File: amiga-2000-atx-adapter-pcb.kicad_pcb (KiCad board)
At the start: 2 copper layers, 99.9 x 63.8 mm, 33 parts, among them J1 ATX-24, J121 12V, J18 PU-18, J2 5.25" PWR, J20 A2000 Power, J21 3.5" PWR, J22 3.5" PWR, J23 3.5" PWR, J24 3.5" PWR, J3 PWR ON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

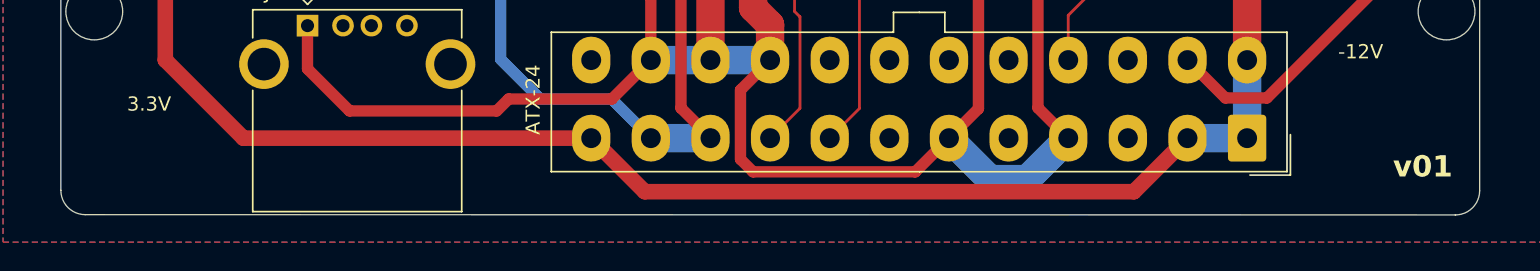
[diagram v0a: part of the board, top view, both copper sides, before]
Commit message: v02: Add ground pad
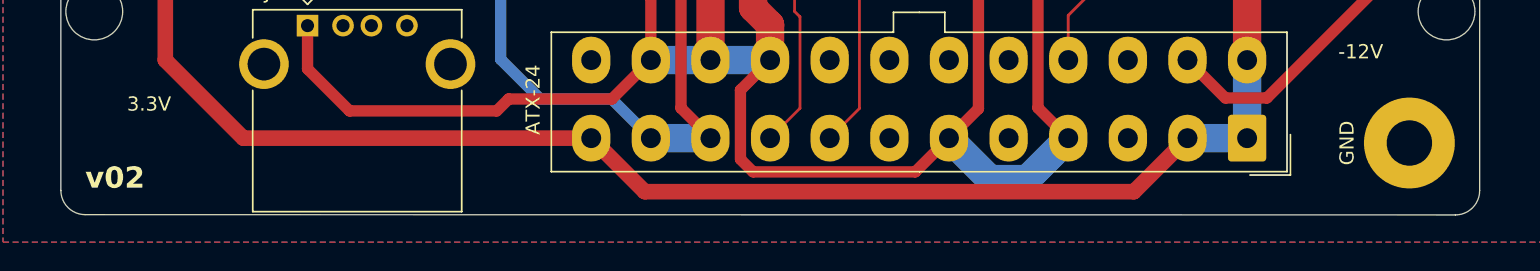
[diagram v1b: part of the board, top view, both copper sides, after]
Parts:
- added H5: MountingHole_Pad, MountingHole:MountingHole_3.2mm_M3_Pad, F.Cu at (218.4, 132.1)
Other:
- board text added: "GND"
- board text added: "v02"
- board text removed: "v01"
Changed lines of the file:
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@@
 		)
 	)
+	(footprint "MountingHole:MountingHole_3.2mm_M3_Pad"
+		(layer "F.Cu")
+		(at 218.44 132.08)
+		(descr "Mounting Hole 3.2mm, M3")
+		(tags "mounting hole 3.2mm m3")
+		(property "Reference" "H5"
+			(at 0 -4.2 0)
+			(layer "F.SilkS")
+			(hide yes)
+			(effects
+				(font
+					(size 1 1)
+					(thickness 0.15)
+				)
+			)
+		)
+		(property "Value" "MountingHole_Pad"
+			(at 0 4.2 0)
+			(layer "F.Fab")
+			(hide yes)
+			(effects
+				(font
+					(size 1 1)
+					(thickness 0.15)
+				)
+			)
+		)
+		(property "Footprint" "MountingHole:MountingHole_3.2mm_M3_Pad"
+			(at 0 0 0)
+			(unlocked yes)
+			(layer "F.Fab")
+			(hide yes)
+			(effects
+				(font
+					(size 1.27 1.27)
+					(thickness 0.15)
+				)
+			)
+		)
+		(property "Datasheet" ""
+			(at 0 0 0)
+			(unlocked yes)
+			(layer "F.Fab")
+			(hide yes)
+			(effects
+				(font
+					(size 1.27 1.27)
+					(thickness 0.15)
+				)
+			)
+		)
+		(property "Description" "Mounting Hole with connection"
+			(at 0 0 0)
+			(unlocked yes)
+			(layer "F.Fab")
+			(hide yes)
+			(effects
+				(font
+					(size 1.27 1.27)
+					(thickness 0.15)
+				)
+			)
+		)
+		(property ki_fp_filters "MountingHole*Pad*")
+		(sheetname "Root")
+		(sheetfile "amiga-2000-atx-adapter-pcb.kicad_sch")
+		(attr exclude_from_pos_files exclude_from_bom)
+		(fp_circle
+			(center 0 0)
+			(end 3.2 0)
+			(stroke
+				(width 0.15)
+				(type solid)
+			)
+			(fill none)
+			(layer "Cmts.User")
+		)
+		(fp_circle
+			(center 0 0)
+			(end 3.45 0)
+			(stroke
+				(width 0.05)
+				(type solid)
+			)
+			(fill none)
+			(layer "F.CrtYd")
+		)
+		(fp_text user "${REFERENCE}"
+			(at 0 0 0)
+			(layer "F.Fab")
+			(effects
+				(font
+					(size 1 1)
+					(thickness 0.15)
+				)
+			)
+		)
+		(pad "1" thru_hole circle
+			(at 0 0)
+			(size 6.4 6.4)
+			(drill 3.2)
+			(layers "*.Cu" "*.Mask")
+			(remove_unused_layers no)
+			(net 2 "GND")
+			(pinfunction "1")
+			(pintype "input")
+		)
+	)
 	(footprint "Connector_Molex:Molex_KK-396_A-41791-0014_1x14_P3.96mm_Vertical"
 		(layer "F.Cu")
@@
 		)
 	)
-	(gr_text "v01"
-		(at 221.488 134.62 0)
+	(gr_text "v02"
+		(at 125.1667 135.4135 0)
 		(layer "F.SilkS")
 		(effects
@@
 				(bold yes)
 			)
-			(justify right bottom)
+			(justify left bottom)
 		)
 	)
@@
 		(layer "F.SilkS")
 		(effects
+			(font
+				(size 1 1)
+				(thickness 0.1)
+			)
+			(justify bottom)
+		)
+	)
+	(gr_text "GND"
+		(at 214.63 132.08 90)
+		(layer "F.SilkS")
+		(effects

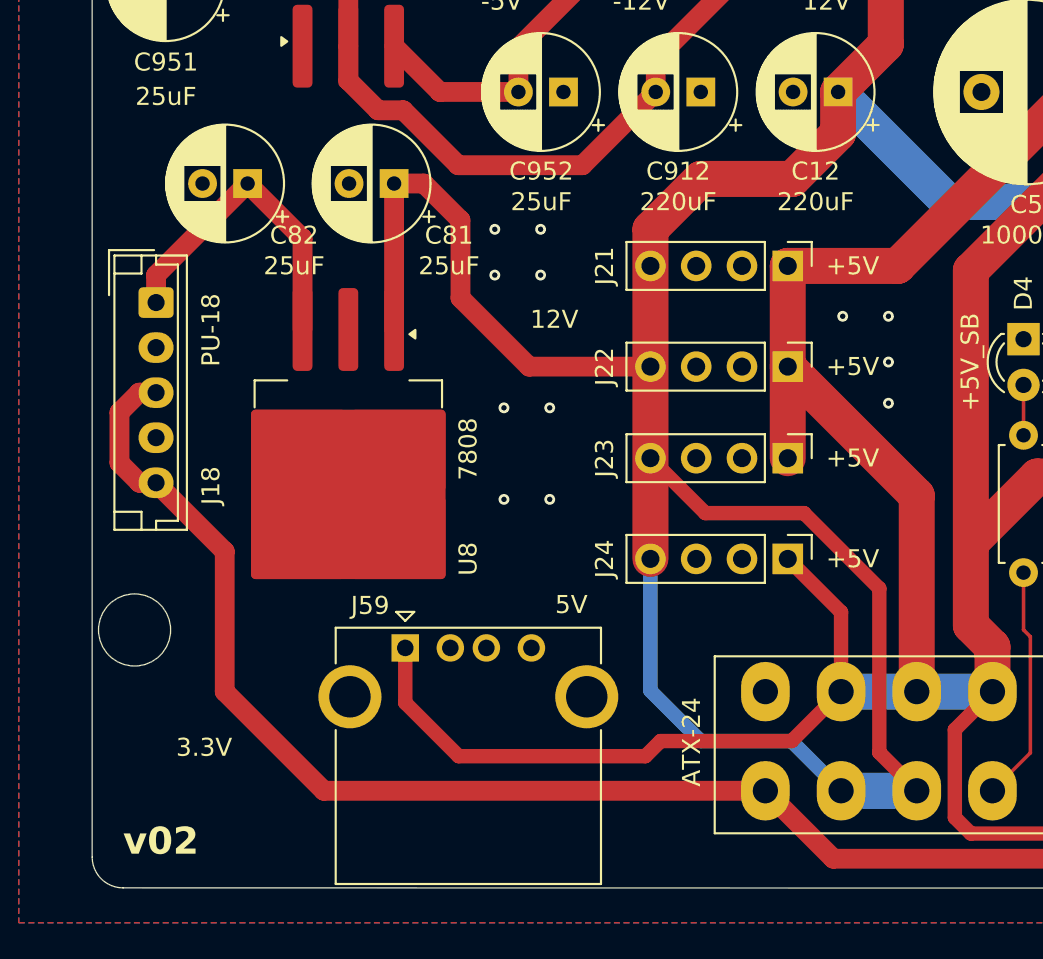
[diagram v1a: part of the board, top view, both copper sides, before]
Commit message: v03: Add PS1 reset switch, remove one 3.5" connector
The 3.5" power connectors were spaced too close together.
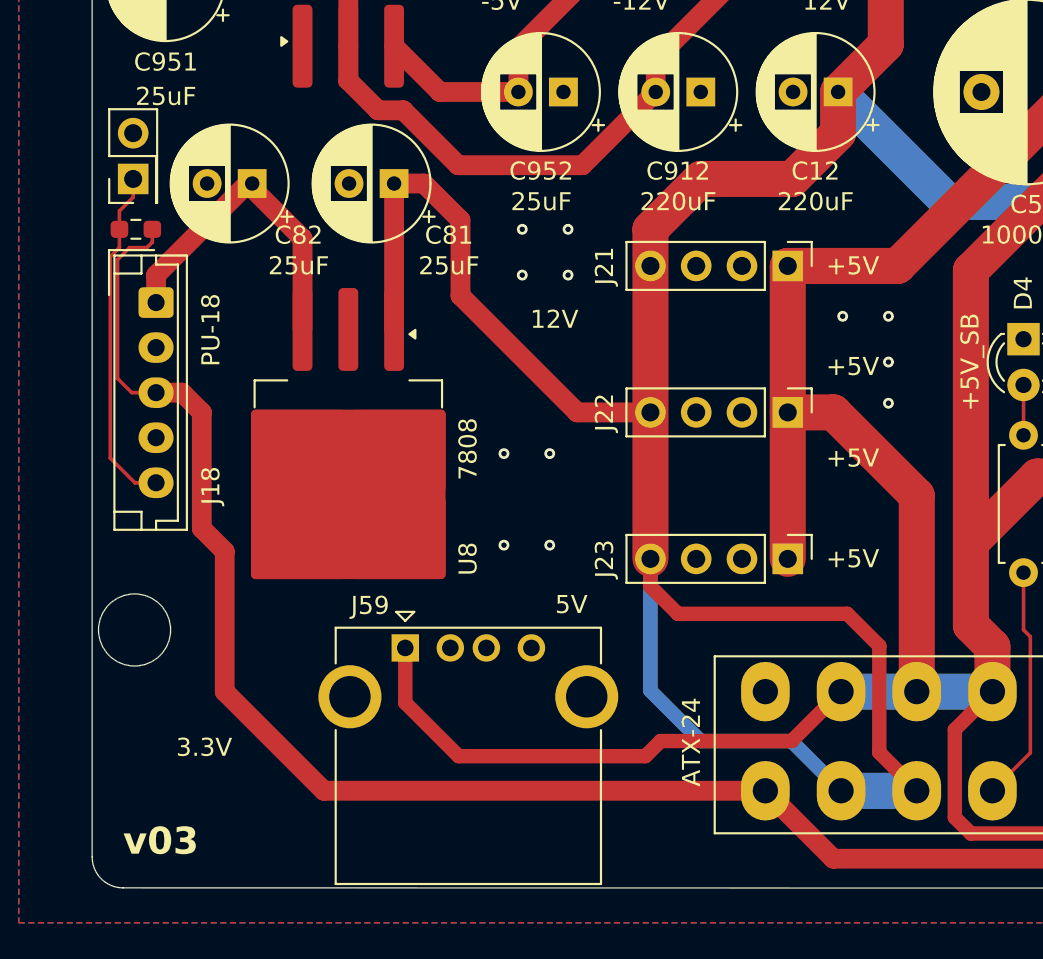
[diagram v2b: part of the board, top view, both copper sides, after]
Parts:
- removed J24: 3.5" PWR, Connector_PinHeader_2.54mm:PinHeader_1x04_P2.54mm_Vertical
- added J19: RESET, Connector_PinHeader_2.54mm:PinHeader_2x01_P2.54mm_Vertical, F.Cu at (125.7, 97.8)
- added R18: 4.7k, Resistor_SMD:R_0603_1608Metric_Pad0.98x0.95mm_HandSolder, F.Cu at (125.9, 100.6)
- moved J23 5.59 mm to (162.1, 118.9)
- moved J22 2.54 mm to (162.1, 110.7)
- moved C82 0.25 mm to (132.3, 98.0)
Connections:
- J18 pad 5: +3.3V -> //RESET
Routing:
- net //RESET: track 0.00 -> 19.1 mm
- net +3.3V: track 131.3 -> 141.5 mm
- net +5V: track 372.0 -> 368.0 mm
- net +12V: track 188.6 -> 186.3 mm
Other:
- board text added: "v03"
- board text removed: "v02"
